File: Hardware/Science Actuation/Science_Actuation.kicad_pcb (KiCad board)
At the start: 2 copper layers, 110 parts, among them J4 RJ45_LED_Shielded, Q1 BSS138, Q2 BSS138, Q3 BSS138, Q4 AO3401A, Q5 AO3401A, SW1 SW_Push, SW10 SW_SPDT, SW2 SW_Push, SW3 SW_Push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

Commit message: Updated Science Actuation PCB
Oriented the board in a better state
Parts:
- moved Conn13 243.3 mm to (30.0, 49.3)
- moved D1 235.8 mm to (28.2, 79.5), turned to 180 degrees
- moved R1 233.1 mm to (32.2, 79.5), turned to 0 degrees
- moved R13 229.3 mm to (28.0, 56.5)
- moved R7 228.3 mm to (31.2, 39.2), turned to 180 degrees
- moved D11 226.8 mm to (27.8, 66.2), turned to 0 degrees
- moved Conn2 226.7 mm to (42.0, 84.8)
- moved D7 226.6 mm to (35.2, 39.2), turned to 180 degrees
- moved R17 226.4 mm to (28.0, 63.4), turned to 0 degrees
- moved Q1 225.9 mm to (32.9, 85.7), turned to 90 degrees
- moved R14 225.1 mm to (28.0, 59.3)
- moved Conn8 223.2 mm to (34.2, 33.1), turned to 180 degrees
- moved R8 221.1 mm to (42.7, 56.4), turned to 180 degrees
- moved R12 220.2 mm to (42.7, 68.1), turned to 180 degrees
- moved R11 220.2 mm to (42.7, 65.3), turned to 180 degrees
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
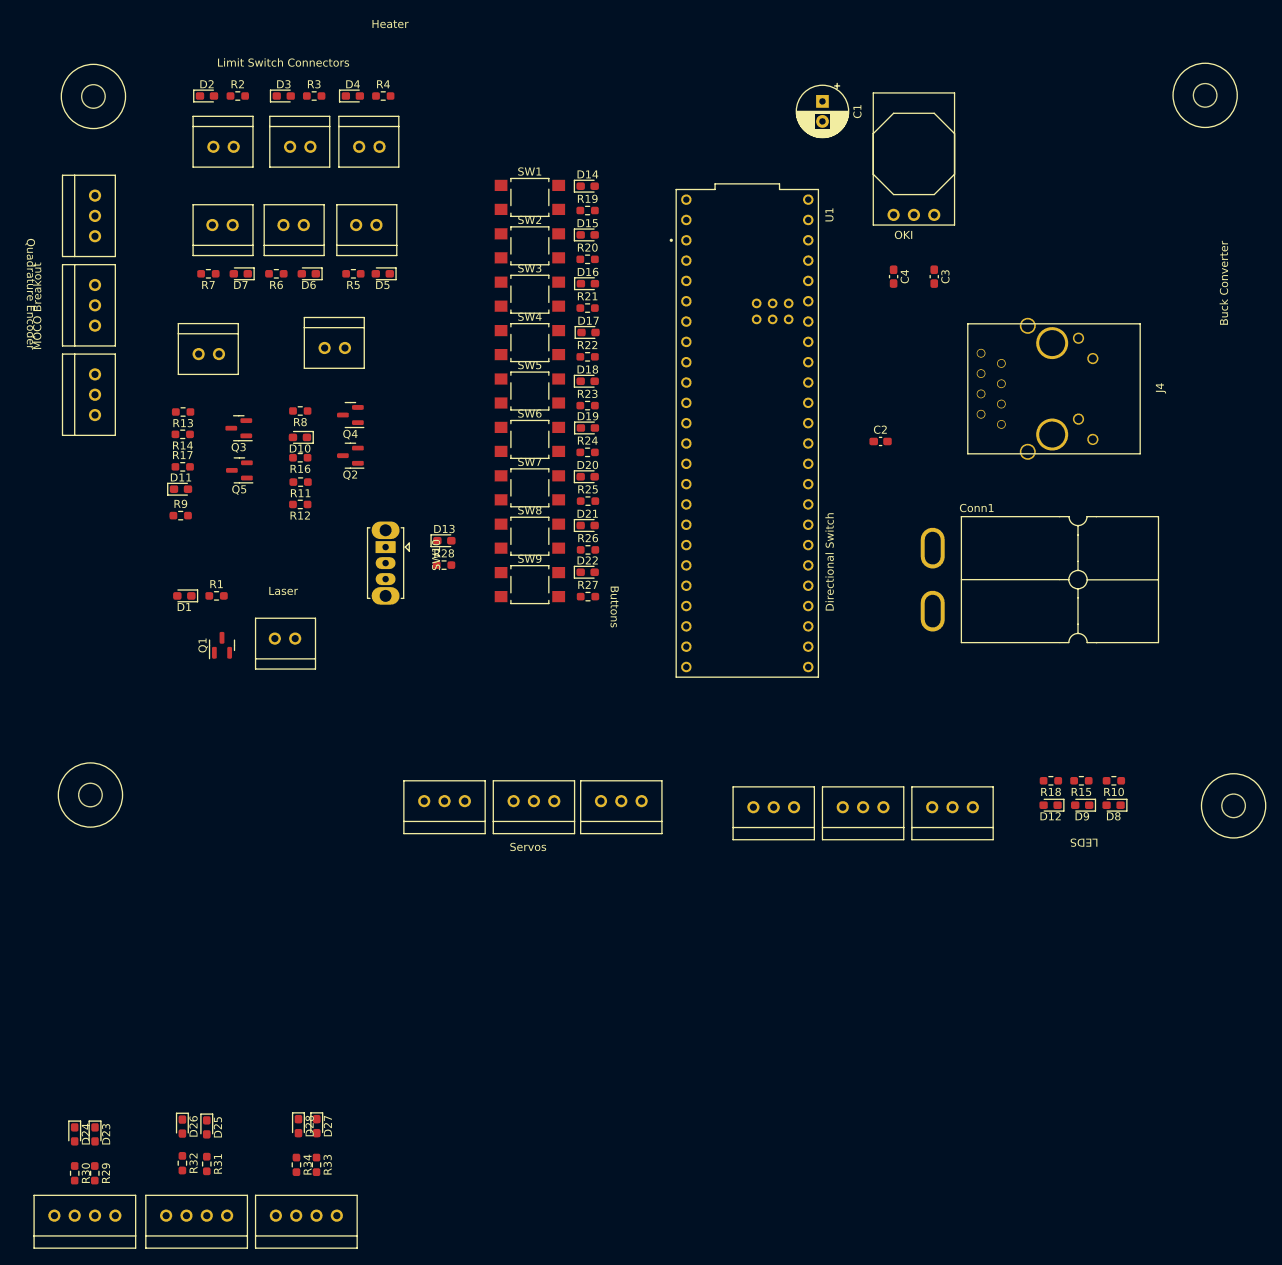
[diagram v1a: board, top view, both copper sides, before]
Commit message: Uploading base template before Traces
Base template before traces. Still need to change what routes everything will connect to the Teensy
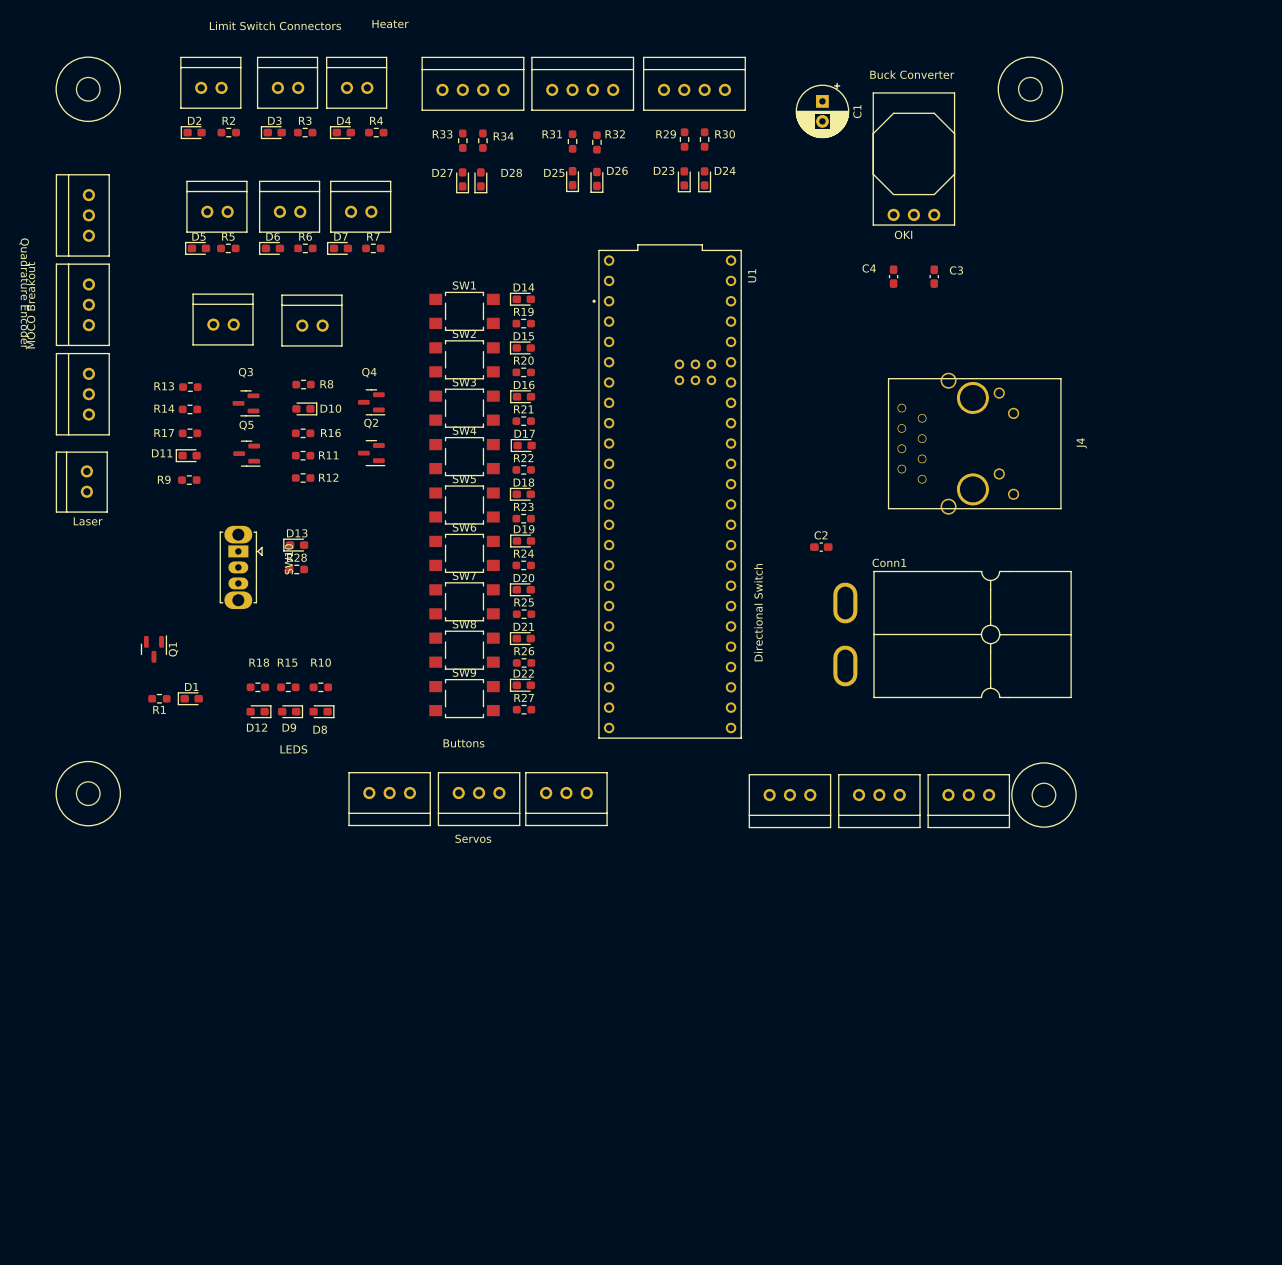
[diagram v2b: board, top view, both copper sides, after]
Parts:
- moved QuadEncode1 156.5 mm to (88.1, 16.3), turned to 0 degrees
- moved R30 151.3 mm to (93.2, 22.5), turned to 90 degrees
- moved R29 148.8 mm to (90.7, 22.5), turned to 90 degrees
- moved QuadEncode2 146.5 mm to (74.2, 16.3), turned to 0 degrees
- moved D24 143.1 mm to (93.2, 27.3), turned to 90 degrees
- moved QuadEncode3 141.3 mm to (60.5, 16.3), turned to 0 degrees
- moved D23 140.4 mm to (90.7, 27.3), turned to 90 degrees
- moved R32 137.7 mm to (79.8, 22.8), turned to 90 degrees
- moved R31 135.7 mm to (76.7, 22.7), turned to 90 degrees
- moved R34 130.1 mm to (65.5, 22.6), turned to 90 degrees
- moved R33 129.3 mm to (63.0, 22.6), turned to 90 degrees
- moved D26 129.3 mm to (79.8, 27.4), turned to 90 degrees
- moved D25 127.2 mm to (76.7, 27.3), turned to 90 degrees
- moved D28 120.5 mm to (65.2, 27.4), turned to 90 degrees
- moved D27 119.7 mm to (63.0, 27.4), turned to 90 degrees
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
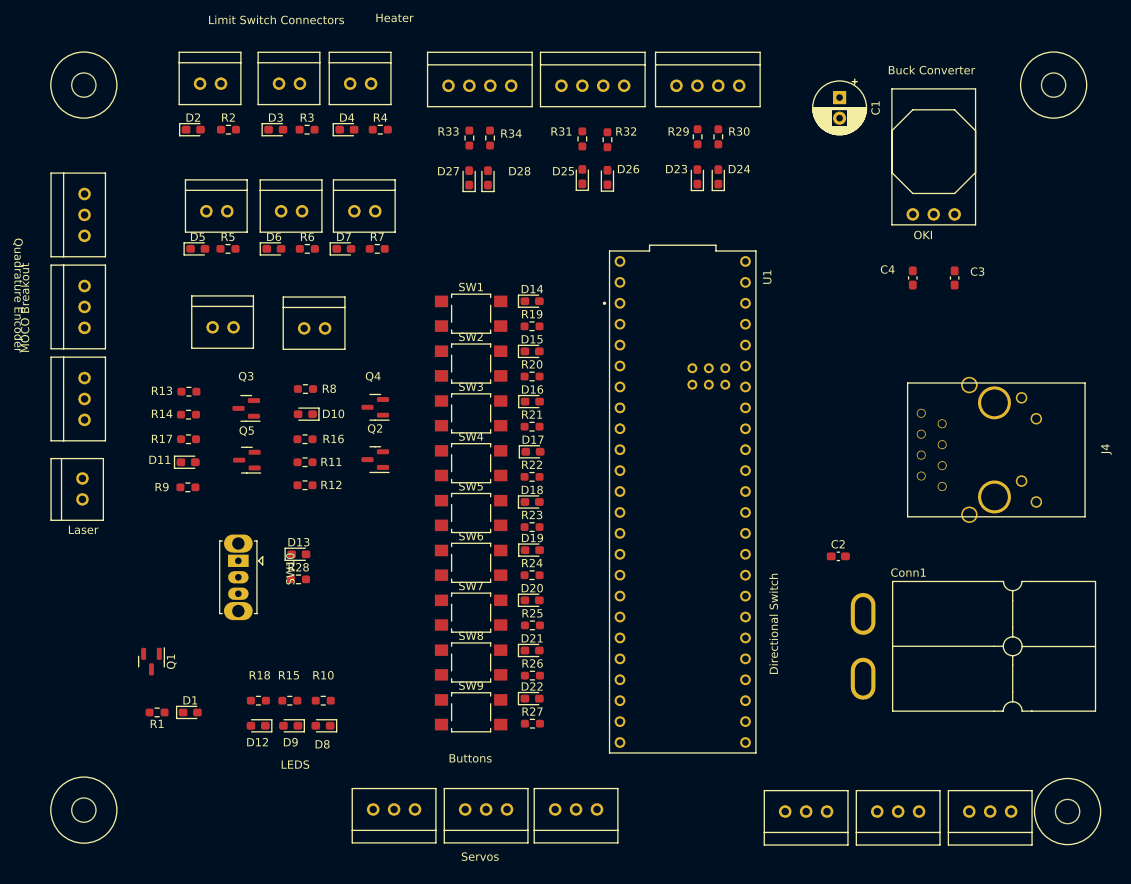
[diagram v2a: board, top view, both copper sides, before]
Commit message: Added traces and changed the layout of the board
Some of it is a mess and will probably be revised later
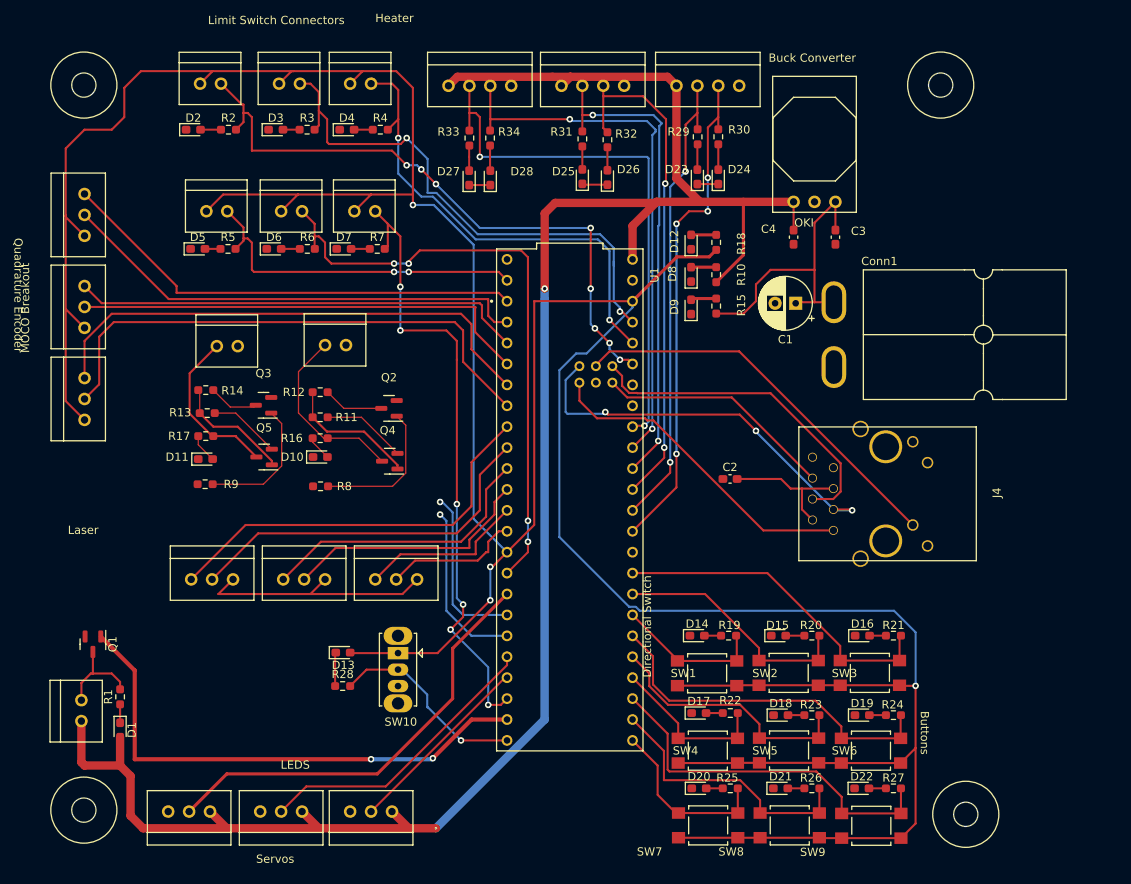
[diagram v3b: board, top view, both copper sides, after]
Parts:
- moved Conn14 103.5 mm to (29.2, 76.2), turned to 0 degrees
- moved Conn15 82.2 mm to (40.4, 76.2), turned to 0 degrees
- moved D12 78.8 mm to (89.9, 35.2), turned to 90 degrees
- moved R18 78.7 mm to (93.0, 35.3), turned to 90 degrees
- moved D8 70.7 mm to (89.9, 39.2), turned to 90 degrees
- moved R15 70.6 mm to (93.0, 43.0), turned to 90 degrees
- moved R10 70.4 mm to (93.0, 39.2), turned to 90 degrees
- moved D9 70.4 mm to (89.9, 43.1), turned to 90 degrees
- moved Conn16 61.7 mm to (51.6, 76.2), turned to 0 degrees
- moved SW3 57.8 mm to (111.6, 87.6), turned to 180 degrees
- moved SW2 53.8 mm to (101.8, 87.6), turned to 180 degrees
- moved SW6 53.7 mm to (111.8, 97.0), turned to 180 degrees
- moved SW1 52.2 mm to (91.9, 87.6), turned to 180 degrees
- moved R21 50.7 mm to (114.5, 83.0), turned to 180 degrees
- moved SW9 50.5 mm to (111.8, 106.1), turned to 180 degrees
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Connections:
- Q3 pad 1: Pump2 -> Pump1
- R9 pad 1: Pump2 -> Pump1
- U1 pad 0: MOCO1_FWD -> LimitSwitch4
- U1 pad 1: MOCO2_FWD -> MOCO3_RVS
- U1 pad 10: unconnected-(U1-CS1-Pad10) -> Heater_On2
- U1 pad 11: Pump1 -> Heater_Temp3
- U1 pad 12: Pump2 -> Heater_On3
- U1 pad 13: Servo_3 -> Encoder_1b
- U1 pad 14: Servo_2 -> Encoder_1a
- U1 pad 15: Servo_1 -> Encoder_2b
- U1 pad 16: SW7 -> Encoder_2a
- U1 pad 17: SW6 -> Encoder_3b
- U1 pad 18: SW5 -> Encoder_3a
- U1 pad 19: SW4 -> unconnected-(U1-A5-Pad19)
- U1 pad 2: Heater_Temp2 -> MOCO3_FWD
- U1 pad 20: SW3 -> unconnected-(U1-A6-Pad20)
- U1 pad 21: SW2 -> LimitSwitch1
- U1 pad 22: SW1 -> LimitSwitch3
- U1 pad 23: Encoder_1a -> LimitSwitch2
- U1 pad 24: Encoder_1b -> LimitSwitch5
- U1 pad 25: Encoder_2a -> Servo_1
- U1 pad 26: Encoder_2b -> Pump1
- U1 pad 27: Encoder_3a -> Pump1
- U1 pad 28: MOCO2_RVS -> Servo_3
- U1 pad 29: MOCO3_RVS -> Servo_2
- U1 pad 3: DIR_SW -> MOCO2_RVS
- U1 pad 30: LimitSwitch3 -> LimitSwitch6
- U1 pad 31: LimitSwitch4 -> LAS
- U1 pad 32: Heater_On3 -> DIR_SW
- U1 pad 33: SW8 -> SW7
- U1 pad 34: LimitSwitch1 -> SW8
- U1 pad 35: LimitSwitch2 -> SW9
- U1 pad 36: LimitSwitch6 -> SW4
- U1 pad 37: LimitSwitch5 -> SW5
- U1 pad 38: Encoder_3b -> SW6
- U1 pad 39: LAS -> SW1
- U1 pad 4: SW9 -> MOCO2_FWD
- U1 pad 40: Heater_Temp -> SW2
- U1 pad 41: Heater_On -> SW3
- U1 pad 5: unconnected-(U1-IN2-Pad5) -> MOCO1_RVS
- U1 pad 6: Heater_Temp3 -> MOCO1_FWD
- U1 pad 7: MOCO3_FWD -> Heater_Temp
- U1 pad 8: MOCO1_RVS -> Heater_On
- U1 pad 9: Heater_On2 -> Heater_Temp2
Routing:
- net +3V3: track 0.00 -> 466.1 mm, vias 0 -> 4
- net +5V: track 0.00 -> 245.6 mm, vias 0 -> 2
- net LimitSwitch1: track 0.00 -> 76.7 mm, vias 0 -> 8
- net LimitSwitch6: track 0.00 -> 76.0 mm, vias 0 -> 6
- net Pump1: track 0.00 -> 74.7 mm, vias 0 -> 2
- net LimitSwitch5: track 0.00 -> 73.8 mm, vias 0 -> 4
- net Encoder_3a: track 0.00 -> 66.5 mm, vias 0 -> 2
- net Encoder_3b: track 0.00 -> 65.9 mm, vias 0 -> 2
- net LimitSwitch2: track 0.00 -> 65.5 mm, vias 0 -> 2
- net MOCO1_FWD: track 0.00 -> 65.0 mm
- net LAS: track 0.00 -> 63.8 mm, vias 0 -> 2
- net MOCO1_RVS: track 0.00 -> 62.5 mm
- net Encoder_2b: track 0.00 -> 61.3 mm, vias 0 -> 2
- net Encoder_1b: track 0.00 -> 61.2 mm, vias 0 -> 4
- net Encoder_2a: track 0.00 -> 59.0 mm, vias 0 -> 2
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
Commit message: Temporary state
Removed things. Added a motor. WIP
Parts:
- added Conn17: Molex_SL_03, MRDT_Connectors:MOLEX_SL_03_Vertical, F.Cu at (38.6, 50.3)
- moved Conn16 56.2 mm to (18.5, 30.7), turned to 90 degrees
- moved Conn15 40.7 mm to (18.5, 41.9), turned to 90 degrees
- moved Conn9 34.2 mm to (49.8, 50.3), turned to 180 degrees
- moved R28 33.1 mm to (75.9, 106.3), turned to 90 degrees
- moved Conn12 32.6 mm to (17.8, 65.0), turned to 90 degrees
- moved D13 32.2 mm to (71.8, 106.3), turned to 90 degrees
- moved Q2 30.9 mm to (23.2, 62.8), turned to -90 degrees
- moved Conn11 30.0 mm to (44.7, 43.9), turned to 0 degrees
- moved Q4 29.8 mm to (24.2, 68.1), turned to 0 degrees
- moved Conn13 29.2 mm to (17.8, 73.2), turned to 90 degrees
- moved Conn14 25.5 mm to (18.5, 53.1), turned to 90 degrees
- moved Q3 24.5 mm to (22.9, 74.4), turned to -90 degrees
- moved SW10 23.4 mm to (71.9, 100.6), turned to 0 degrees
- moved D5 21.9 mm to (51.9, 35.6), turned to 180 degrees
- moved R7 21.7 mm to (30.1, 35.6), turned to 180 degrees
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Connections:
- Conn14 pad 3: +3.3V -> +3V3
- Conn15 pad 3: +3.3V -> +3V3
- Conn16 pad 3: +3.3V -> +3V3
- Q3 pad 1: Pump1 -> Pump2
- R9 pad 1: Pump1 -> Pump2
- U1 pad 19: unconnected-(U1-A5-Pad19) -> SW6
- U1 pad 20: unconnected-(U1-A6-Pad20) -> MOCO3_FWD
- U1 pad 26: Pump1 -> Pump2
- U1 pad 38: SW6 -> MOCO3_RVS
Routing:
- net MOCO3_RVS: track 57.2 -> 1.44 mm
- net MOCO3_FWD: track 57.9 -> 4.63 mm
- net MOCO1_FWD: track 65.0 -> 12.8 mm
- net Pump1: track 74.7 -> 22.9 mm, vias 2 -> 1
- net MOCO1_RVS: track 62.5 -> 11.0 mm
- net MOCO2_RVS: track 55.1 -> 6.21 mm
- net MOCO2_FWD: track 56.1 -> 8.62 mm
- net Heater_Temp: track 49.2 -> 14.7 mm
- net Heater_On: track 45.0 -> 12.9 mm
- net +3.3V: track 29.9 -> 0.00 mm
- net Heater_Temp2: track 34.7 -> 11.2 mm
- net Net-(Q4-D): track 22.2 -> 0.00 mm
- net Heater_On2: track 30.6 -> 9.43 mm
- net LimitSwitch6: track 76.0 -> 96.7 mm, vias 6 -> 4
- net Pump2: track 0.00 -> 20.4 mm
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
